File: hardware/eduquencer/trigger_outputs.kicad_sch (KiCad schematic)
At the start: 2 parts

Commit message: Hardware: add test points, tiny cleanup
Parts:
- added J?: Out 2, AudioJacks:Jack_3.5mm_QingPu_WQP-PJ301BM_Vertical, symbol Connector:AudioJack2_SwitchT
- added J?: Out 4, AudioJacks:Jack_3.5mm_QingPu_WQP-PJ301BM_Vertical, symbol Connector:AudioJack2_SwitchT
- added J?: Out 6, AudioJacks:Jack_3.5mm_QingPu_WQP-PJ301BM_Vertical, symbol Connector:AudioJack2_SwitchT
- added J?: Out 5, AudioJacks:Jack_3.5mm_QingPu_WQP-PJ301BM_Vertical, symbol Connector:AudioJack2_SwitchT
- added J?: Out 3, AudioJacks:Jack_3.5mm_QingPu_WQP-PJ301BM_Vertical, symbol Connector:AudioJack2_SwitchT
- added J?: Out 7, AudioJacks:Jack_3.5mm_QingPu_WQP-PJ301BM_Vertical, symbol Connector:AudioJack2_SwitchT
- added J?: Out 1, AudioJacks:Jack_3.5mm_QingPu_WQP-PJ301BM_Vertical, symbol Connector:AudioJack2_SwitchT
- added R? (x7): 1k, symbol Device:R_Small
- C?: LCSC C14663 -> (none); LCSC Part # C14663 -> (none)
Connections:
- net GND: now also J?.S, J?.S, J?.S, J?.S, J?.S, J?.S, J?.S
- net trig_1_out_h renamed trig_out0
- net trig_out0: now also R?.1
- net trig_1_out_l renamed trig_out_a
- net trig_2_out_h renamed trig_out1
- net trig_out1: now also R?.1
- net trig_2_out_l renamed trig_out_b
- net trig_3_out_h renamed trig_out2
- net trig_out2: now also R?.1
- net trig_3_out_l renamed trig_out_c
- net trig_4_out_h renamed trig_out3
- net trig_out3: now also R?.1
- net trig_4_out_l renamed trig_out_d
- net trig_5_out_h: no longer names the net of IC?.3 (2Y4)
- net trig_5_out_l: no longer names the net of IC?.17 (2A4)
- net trig_6_out_h renamed trig_out6
- net trig_out6: now also R?.1
- net trig_6_out_l renamed trig_out_g
- net trig_7_out_h renamed trig_out5
- net trig_out5: now also R?.1
- net trig_7_out_l renamed trig_out_f
- net trig_8_out_l renamed trig_out4
- net trig_out4: now also R?.1; no longer IC?.11 (2A1)
- new net: J?.T, R?.2 (x7)
- new net trig_out_e: IC?.11 (2A1)
- no-connect marks 0 -> 9
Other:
- note removed: "TODO: use a bus for inputs. outputs should be named trig_out_a, trig_out_b, etc."
- moved on the sheet: C?

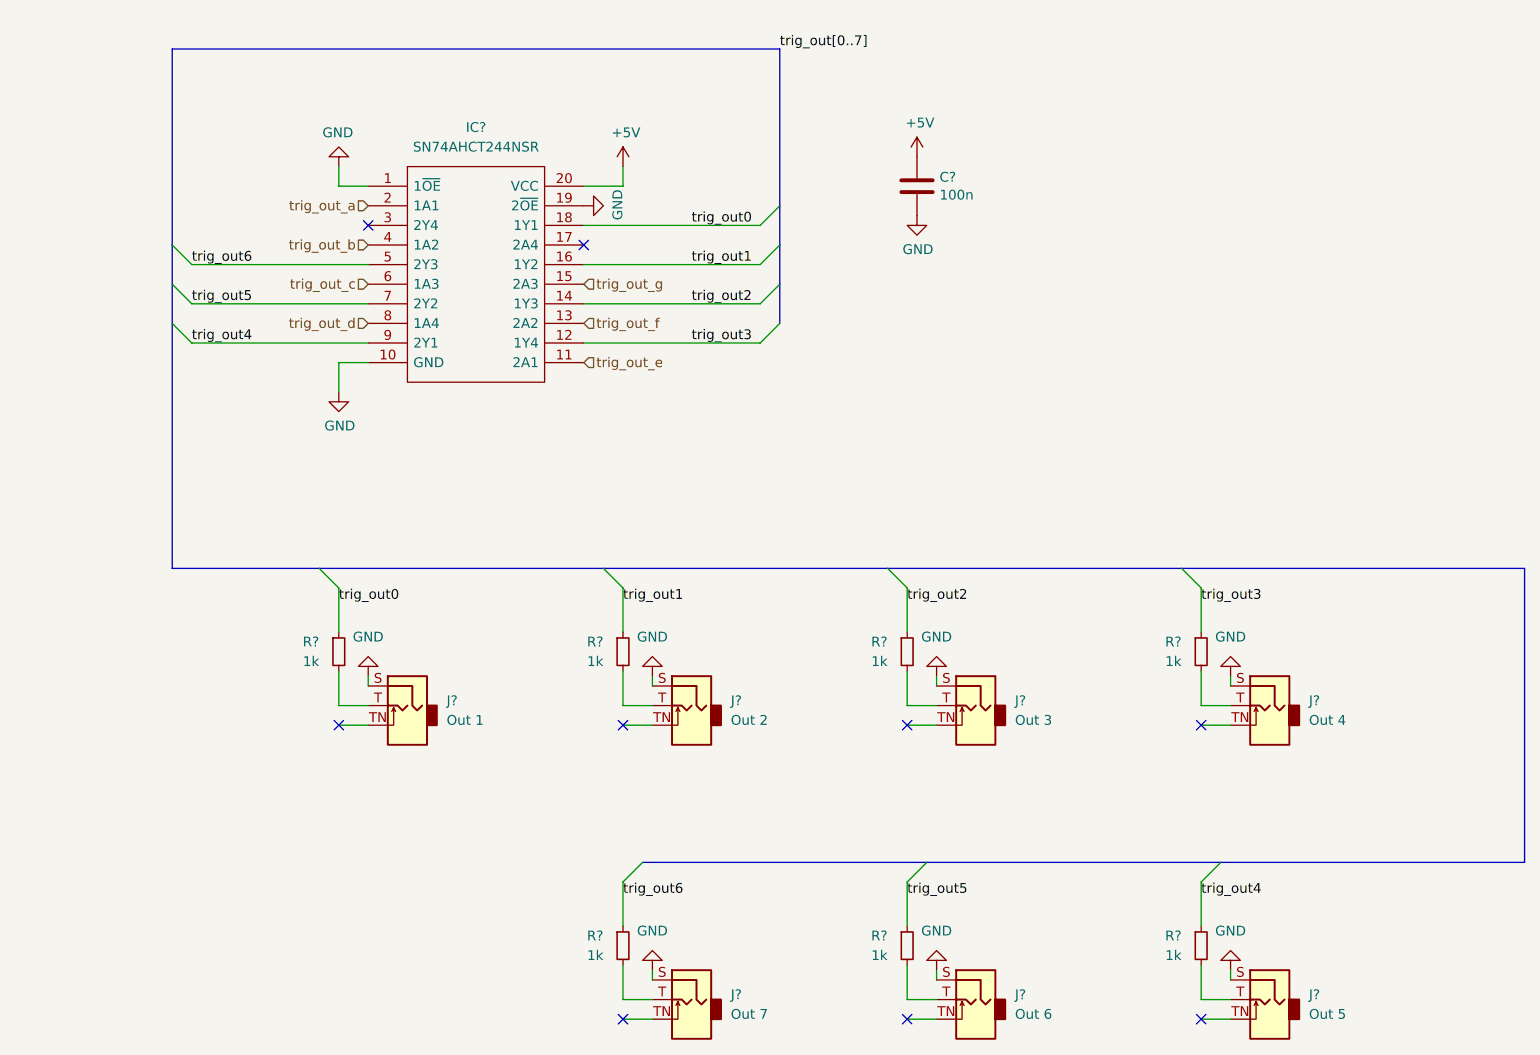
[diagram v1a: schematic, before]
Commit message: Hardware: update models, annotate, fix ERC issues
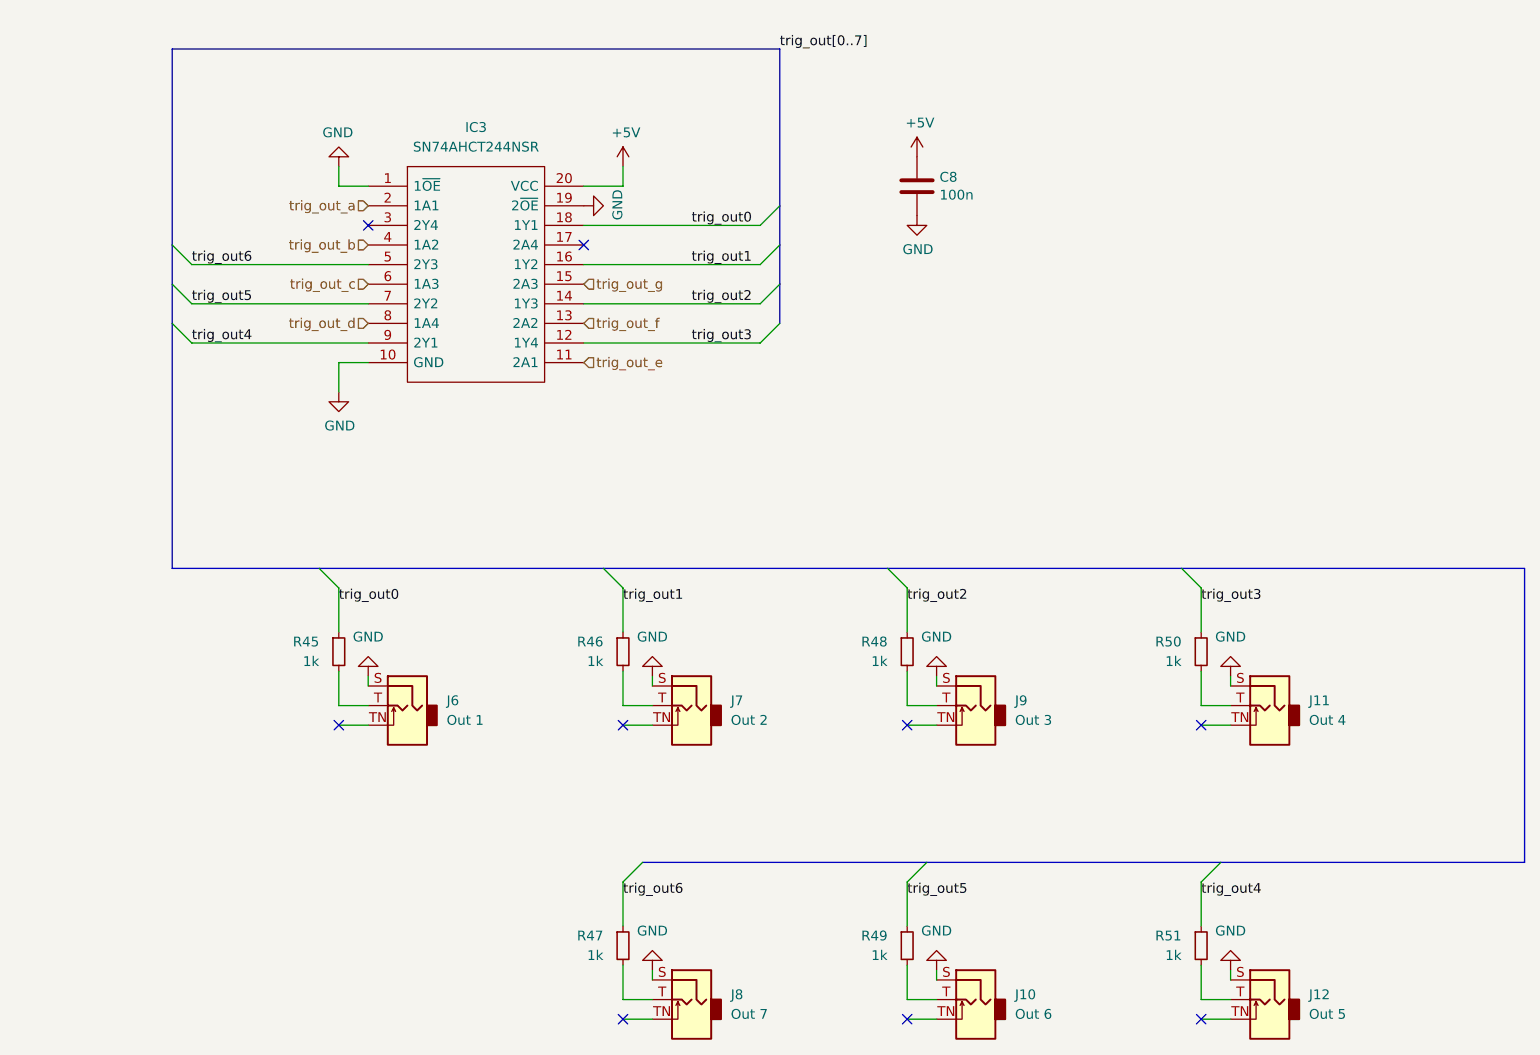
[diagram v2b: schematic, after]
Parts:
- gave numbers to parts that had none: 16
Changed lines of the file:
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@@
   (symbol (lib_id "Connector:AudioJack2_SwitchT") (at 116.84 113.03 0) (mirror y) (unit 1)
     (in_bom yes) (on_board yes) (fields_autoplaced)
-    (property "Reference" "J?" (id 0) (at 121.92 112.3949 0)
+    (property "Reference" "J7" (id 0) (at 121.92 112.3949 0)
       (effects (font (size 1.27 1.27)) (justify right))
     )
@@
   (symbol (lib_id "Connector:AudioJack2_SwitchT") (at 191.77 113.03 0) (mirror y) (unit 1)
     (in_bom yes) (on_board yes) (fields_autoplaced)
-    (property "Reference" "J?" (id 0) (at 196.85 112.3949 0)
+    (property "Reference" "J11" (id 0) (at 196.85 112.3949 0)
       (effects (font (size 1.27 1.27)) (justify right))
     )
@@
   (symbol (lib_id "Device:R_Small") (at 107.95 106.045 0) (unit 1)
     (in_bom yes) (on_board yes)
-    (property "Reference" "R?" (id 0) (at 105.41 104.775 0)
+    (property "Reference" "R46" (id 0) (at 105.41 104.775 0)
       (effects (font (size 1.27 1.27)) (justify right))
     )
@@
   (symbol (lib_id "Device:R_Small") (at 107.95 144.145 0) (unit 1)
     (in_bom yes) (on_board yes)
-    (property "Reference" "R?" (id 0) (at 105.41 142.875 0)
+    (property "Reference" "R47" (id 0) (at 105.41 142.875 0)
       (effects (font (size 1.27 1.27)) (justify right))
     )
@@
   (symbol (lib_id "Device:R_Small") (at 182.88 106.045 0) (unit 1)
     (in_bom yes) (on_board yes)
-    (property "Reference" "R?" (id 0) (at 180.34 104.775 0)
+    (property "Reference" "R50" (id 0) (at 180.34 104.775 0)
       (effects (font (size 1.27 1.27)) (justify right))
     )
@@
   (symbol (lib_id "Connector:AudioJack2_SwitchT") (at 153.67 151.13 0) (mirror y) (unit 1)
     (in_bom yes) (on_board yes) (fields_autoplaced)
-    (property "Reference" "J?" (id 0) (at 158.75 150.4949 0)
+    (property "Reference" "J10" (id 0) (at 158.75 150.4949 0)
       (effects (font (size 1.27 1.27)) (justify right))
     )
@@
   (symbol (lib_id "Device:R_Small") (at 144.78 144.145 0) (unit 1)
     (in_bom yes) (on_board yes)
-    (property "Reference" "R?" (id 0) (at 142.24 142.875 0)
+    (property "Reference" "R49" (id 0) (at 142.24 142.875 0)
       (effects (font (size 1.27 1.27)) (justify right))
     )
@@
   (symbol (lib_id "Connector:AudioJack2_SwitchT") (at 191.77 151.13 0) (mirror y) (unit 1)
     (in_bom yes) (on_board yes) (fields_autoplaced)
-    (property "Reference" "J?" (id 0) (at 196.85 150.4949 0)
+    (property "Reference" "J12" (id 0) (at 196.85 150.4949 0)
       (effects (font (size 1.27 1.27)) (justify right))
     )
@@
   (symbol (lib_id "SN74AHCT244NSR:SN74AHCT244NSR") (at 74.93 45.72 0) (unit 1)
     (in_bom yes) (on_board yes) (fields_autoplaced)
-    (property "Reference" "IC?" (id 0) (at 88.9 38.1 0))
+    (property "Reference" "IC3" (id 0) (at 88.9 38.1 0))
     (property "Value" "SN74AHCT244NSR" (id 1) (at 88.9 40.64 0))
     (property "Footprint" "SOIC127P780X200-20N" (id 2) (at 99.06 43.18 0)
@@
   (symbol (lib_id "Connector:AudioJack2_SwitchT") (at 153.67 113.03 0) (mirror y) (unit 1)
     (in_bom yes) (on_board yes) (fields_autoplaced)
-    (property "Reference" "J?" (id 0) (at 158.75 112.3949 0)
+    (property "Reference" "J9" (id 0) (at 158.75 112.3949 0)
       (effects (font (size 1.27 1.27)) (justify right))
     )
@@
   (symbol (lib_id "Device:R_Small") (at 182.88 144.145 0) (unit 1)
     (in_bom yes) (on_board yes)
-    (property "Reference" "R?" (id 0) (at 180.34 142.875 0)
+    (property "Reference" "R51" (id 0) (at 180.34 142.875 0)
       (effects (font (size 1.27 1.27)) (justify right))
     )
@@
   (symbol (lib_id "Device:R_Small") (at 144.78 106.045 0) (unit 1)
     (in_bom yes) (on_board yes)
-    (property "Reference" "R?" (id 0) (at 142.24 104.775 0)
+    (property "Reference" "R48" (id 0) (at 142.24 104.775 0)
       (effects (font (size 1.27 1.27)) (justify right))
     )
@@
   (symbol (lib_id "Device:C") (at 146.05 45.72 0) (unit 1)
     (in_bom yes) (on_board yes)
-    (property "Reference" "C?" (id 0) (at 148.971 44.5516 0)
+    (property "Reference" "C8" (id 0) (at 148.971 44.5516 0)
       (effects (font (size 1.27 1.27)) (justify left))
     )
@@
   (symbol (lib_id "Connector:AudioJack2_SwitchT") (at 116.84 151.13 0) (mirror y) (unit 1)
     (in_bom yes) (on_board yes) (fields_autoplaced)
-    (property "Reference" "J?" (id 0) (at 121.92 150.4949 0)
+    (property "Reference" "J8" (id 0) (at 121.92 150.4949 0)
       (effects (font (size 1.27 1.27)) (justify right))
     )
@@
   (symbol (lib_id "Connector:AudioJack2_SwitchT") (at 80.01 113.03 0) (mirror y) (unit 1)
     (in_bom yes) (on_board yes) (fields_autoplaced)
-    (property "Reference" "J?" (id 0) (at 85.09 112.3949 0)
+    (property "Reference" "J6" (id 0) (at 85.09 112.3949 0)
       (effects (font (size 1.27 1.27)) (justify right))
     )
@@
   (symbol (lib_id "Device:R_Small") (at 71.12 106.045 0) (unit 1)
     (in_bom yes) (on_board yes)
-    (property "Reference" "R?" (id 0) (at 68.58 104.775 0)
-      (effects (font (size 1.27 1.27)) (justify right))
-    )
+    (property "Reference" "R45" (id 0) (at 68.58 104.775 0)
+      (effects (font (size 1.27 1.27)) (justify right))
+    )

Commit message: Hardware: assign all footprints
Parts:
- C8: footprint Capacitor_SMD:C_0603_1608Metric -> Capacitor_SMD:C_0603_1608Metric_Pad1.08x0.95mm_HandSolder
- IC3: footprint SOIC127P780X200-20N -> SN74AHCT244NSR:SOIC127P780X200-20N
- R45, R46, R47, R48, R49, R50, R51: footprint (none) -> Resistor_SMD:R_0603_1608Metric_Pad0.98x0.95mm_HandSolder
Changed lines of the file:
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@@
       (effects (font (size 1.27 1.27)) (justify right))
     )
-    (property "Footprint" "" (id 2) (at 107.95 106.045 0)
+    (property "Footprint" "Resistor_SMD:R_0603_1608Metric_Pad0.98x0.95mm_HandSolder" (id 2) (at 107.95 106.045 0)
       (effects (font (size 1.27 1.27)) hide)
     )
@@
       (effects (font (size 1.27 1.27)) (justify right))
     )
-    (property "Footprint" "" (id 2) (at 107.95 144.145 0)
+    (property "Footprint" "Resistor_SMD:R_0603_1608Metric_Pad0.98x0.95mm_HandSolder" (id 2) (at 107.95 144.145 0)
       (effects (font (size 1.27 1.27)) hide)
     )
@@
       (effects (font (size 1.27 1.27)) (justify right))
     )
-    (property "Footprint" "" (id 2) (at 182.88 106.045 0)
+    (property "Footprint" "Resistor_SMD:R_0603_1608Metric_Pad0.98x0.95mm_HandSolder" (id 2) (at 182.88 106.045 0)
       (effects (font (size 1.27 1.27)) hide)
     )
@@
       (effects (font (size 1.27 1.27)) (justify right))
     )
-    (property "Footprint" "" (id 2) (at 144.78 144.145 0)
+    (property "Footprint" "Resistor_SMD:R_0603_1608Metric_Pad0.98x0.95mm_HandSolder" (id 2) (at 144.78 144.145 0)
       (effects (font (size 1.27 1.27)) hide)
     )
@@
     (property "Reference" "IC3" (id 0) (at 88.9 38.1 0))
     (property "Value" "SN74AHCT244NSR" (id 1) (at 88.9 40.64 0))
-    (property "Footprint" "SOIC127P780X200-20N" (id 2) (at 99.06 43.18 0)
+    (property "Footprint" "SN74AHCT244NSR:SOIC127P780X200-20N" (id 2) (at 99.06 43.18 0)
       (effects (font (size 1.27 1.27)) (justify left) hide)
     )
@@
       (effects (font (size 1.27 1.27)) (justify right))
     )
-    (property "Footprint" "" (id 2) (at 182.88 144.145 0)
+    (property "Footprint" "Resistor_SMD:R_0603_1608Metric_Pad0.98x0.95mm_HandSolder" (id 2) (at 182.88 144.145 0)
       (effects (font (size 1.27 1.27)) hide)
     )
@@
       (effects (font (size 1.27 1.27)) (justify right))
     )
-    (property "Footprint" "" (id 2) (at 144.78 106.045 0)
+    (property "Footprint" "Resistor_SMD:R_0603_1608Metric_Pad0.98x0.95mm_HandSolder" (id 2) (at 144.78 106.045 0)
       (effects (font (size 1.27 1.27)) hide)
     )
@@
       (effects (font (size 1.27 1.27)) (justify left))
     )
-    (property "Footprint" "Capacitor_SMD:C_0603_1608Metric" (id 2) (at 147.0152 49.53 0)
+    (property "Footprint" "Capacitor_SMD:C_0603_1608Metric_Pad1.08x0.95mm_HandSolder" (id 2) (at 147.0152 49.53 0)
       (effects (font (size 1.27 1.27)) hide)
     )
@@
       (effects (font (size 1.27 1.27)) (justify right))
     )
-    (property "Footprint" "" (id 2) (at 71.12 106.045 0)
-      (effects (font (size 1.27 1.27)) hide)
-    )
+    (property "Footprint" "Resistor_SMD:R_0603_1608Metric_Pad0.98x0.95mm_HandSolder" (id 2) (at 71.12 106.045 0)
+      (effects (font (size 1.27 1.27)) hide)
+    )
